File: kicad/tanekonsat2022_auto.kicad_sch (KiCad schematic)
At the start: 52 parts

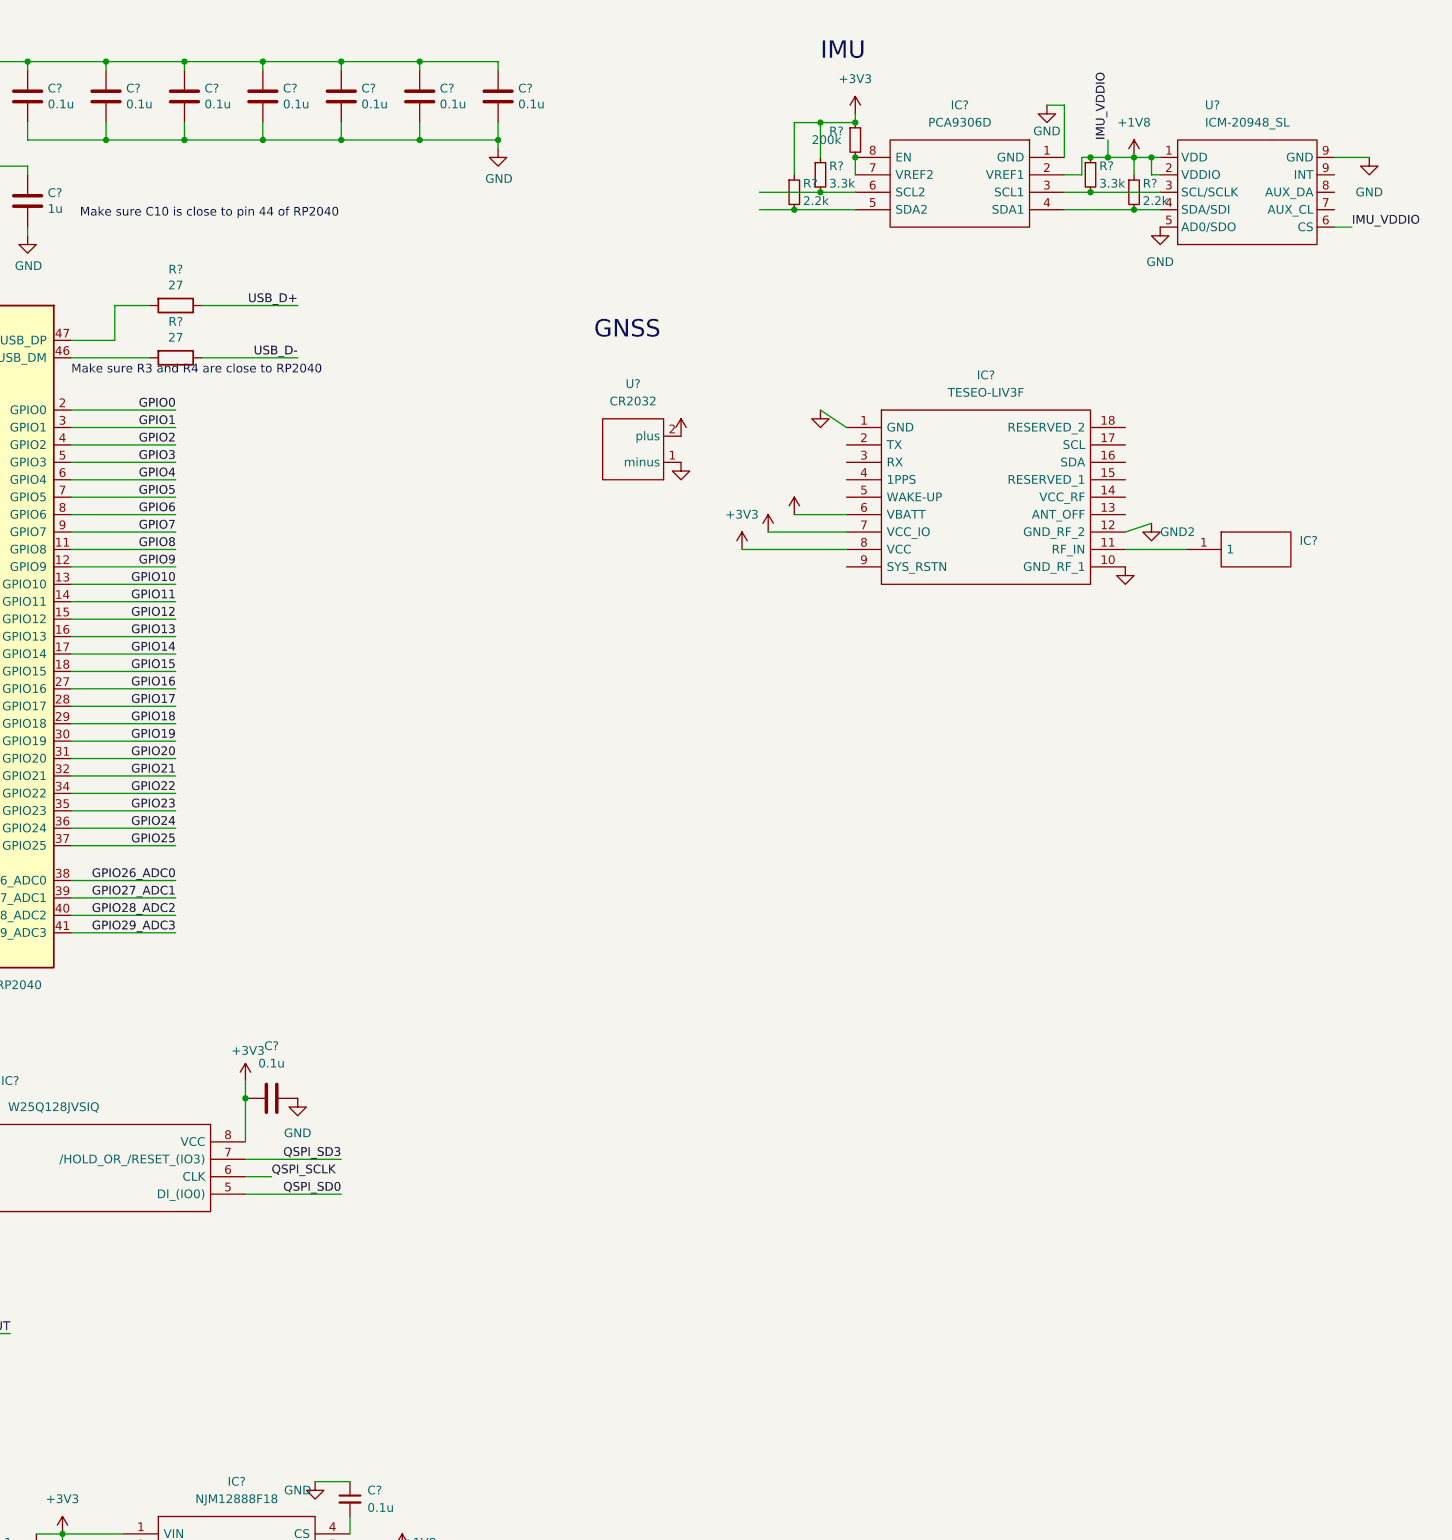
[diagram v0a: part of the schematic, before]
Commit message: update schematic
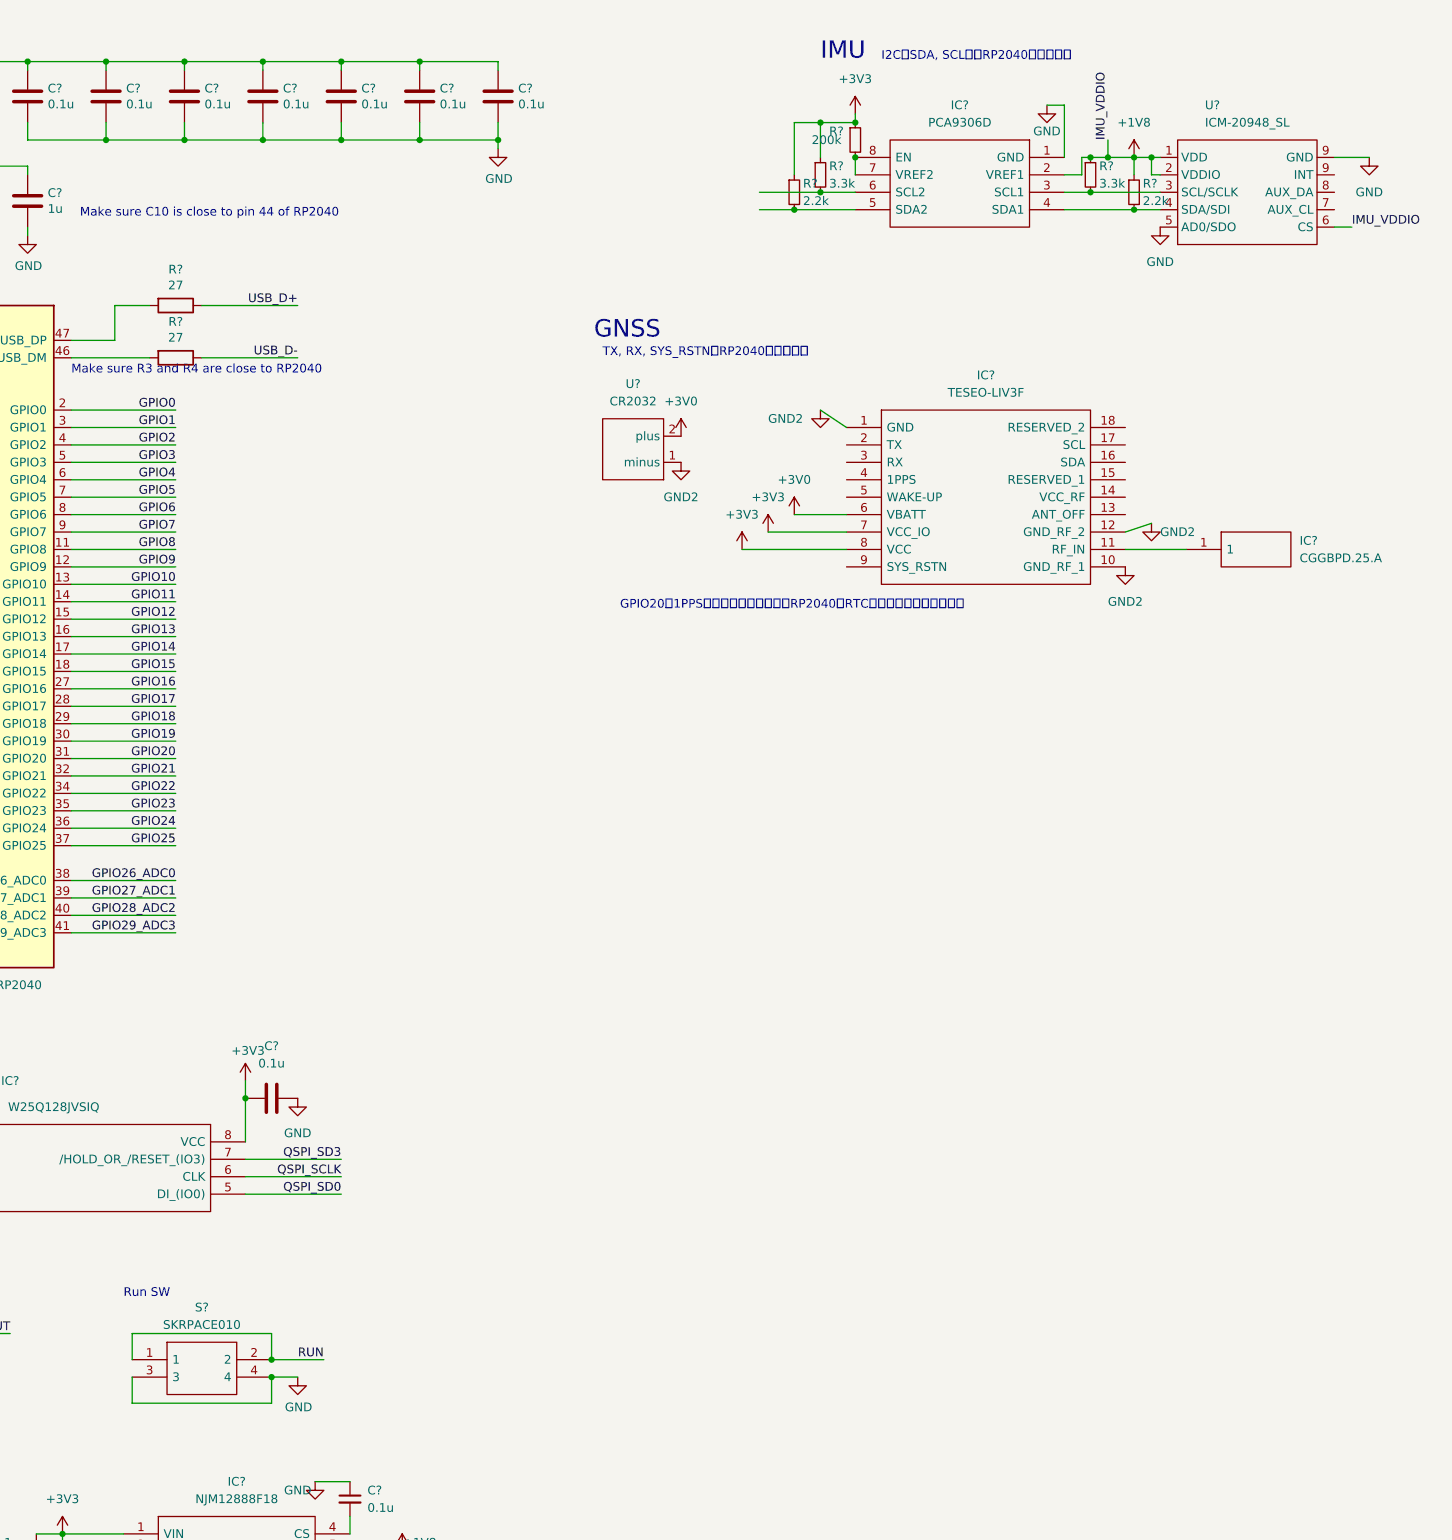
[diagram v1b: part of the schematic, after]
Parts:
- added S?: SKRPACE010, SamacSys_Parts:SMT_4.2X3.2_, symbol SamacSys_Parts:SKRPACE010
- IC?: value (none) -> CGGBPD.25.A; footprint (none) -> CGGBPD25A
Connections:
- net GND: now also S?.3, S?.4
- net RUN: now also S?.1, S?.2
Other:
- note added: "GPIO20に1PPSの信号を突っ込めば，RP2040のRTCがより高精度になるぽい"
- note added: "I2C（SDA, SCL）をRP2040と接続する"
- note added: "Run SW"
- note added: "TX, RX, SYS_RSTNをRP2040と接続する"
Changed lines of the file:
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@@
   (junction (at 252.73 38.1) (diameter 0) (color 0 0 0 0)
   )
+  (junction (at 124.46 213.36) (diameter 0) (color 0 0 0 0)
+  )
   (junction (at 35.56 259.08) (diameter 0) (color 0 0 0 0)
   )
@@
   (junction (at 123.19 35.56) (diameter 0) (color 0 0 0 0)
   )
+  (junction (at 124.46 215.9) (diameter 0) (color 0 0 0 0)
+  )
   (junction (at 123.19 24.13) (diameter 0) (color 0 0 0 0)
   )
@@
     (stroke (width 0) (type default) (color 0 0 0 0))
   )
+  (wire (pts (xy 104.14 219.71) (xy 104.14 215.9))
+    (stroke (width 0) (type default) (color 0 0 0 0))
+  )
   (wire (pts (xy 95.25 118.11) (xy 110.49 118.11))
     (stroke (width 0) (type default) (color 0 0 0 0))
@@
     (stroke (width 0) (type default) (color 0 0 0 0))
   )
+  (wire (pts (xy 128.27 215.9) (xy 124.46 215.9))
+    (stroke (width 0) (type default) (color 0 0 0 0))
+  )
   (wire (pts (xy 196.85 92.71) (xy 208.28 92.71))
     (stroke (width 0) (type default) (color 0 0 0 0))
@@
     (stroke (width 0) (type default) (color 0 0 0 0))
   )
+  (wire (pts (xy 124.46 215.9) (xy 124.46 219.71))
+    (stroke (width 0) (type default) (color 0 0 0 0))
+  )
   (wire (pts (xy 46.99 276.86) (xy 46.99 278.13))
     (stroke (width 0) (type default) (color 0 0 0 0))
@@
     (stroke (width 0) (type default) (color 0 0 0 0))
   )
+  (wire (pts (xy 132.08 213.36) (xy 124.46 213.36))
+    (stroke (width 0) (type default) (color 0 0 0 0))
+  )
   (wire (pts (xy 120.65 172.72) (xy 120.65 175.26))
     (stroke (width 0) (type default) (color 0 0 0 0))
@@
     (stroke (width 0) (type default) (color 0 0 0 0))
   )
+  (wire (pts (xy 124.46 209.55) (xy 124.46 213.36))
+    (stroke (width 0) (type default) (color 0 0 0 0))
+  )
   (wire (pts (xy 77.47 265.43) (xy 77.47 266.7))
     (stroke (width 0) (type default) (color 0 0 0 0))
@@
     (stroke (width 0) (type default) (color 0 0 0 0))
   )
+  (wire (pts (xy 124.46 209.55) (xy 104.14 209.55))
+    (stroke (width 0) (type default) (color 0 0 0 0))
+  )
   (wire (pts (xy 80.01 24.13) (xy 80.01 39.37))
     (stroke (width 0) (type default) (color 0 0 0 0))
@@
     (stroke (width 0) (type default) (color 0 0 0 0))
   )
+  (wire (pts (xy 124.46 219.71) (xy 104.14 219.71))
+    (stroke (width 0) (type default) (color 0 0 0 0))
+  )
   (wire (pts (xy 95.25 123.19) (xy 110.49 123.19))
     (stroke (width 0) (type default) (color 0 0 0 0))
@@
     (stroke (width 0) (type default) (color 0 0 0 0))
   )
+  (wire (pts (xy 104.14 209.55) (xy 104.14 213.36))
+    (stroke (width 0) (type default) (color 0 0 0 0))
+  )
   (wire (pts (xy 17.78 80.01) (xy 31.75 80.01))
     (stroke (width 0) (type default) (color 0 0 0 0))
@@
     (stroke (width 0) (type default) (color 0 0 0 0))
   )
-  (wire (pts (xy 124.46 186.69) (xy 120.65 186.69))
+  (wire (pts (xy 134.62 186.69) (xy 120.65 186.69))
     (stroke (width 0) (type default) (color 0 0 0 0))
   )
@@
     (effects (font (size 1.27 1.27)) (justify left bottom))
   )
+  (text "TX, RX, SYS_RSTNをRP2040と接続する" (at 172.72 67.31 0)
+    (effects (font (size 1.27 1.27)) (justify left bottom))
+  )
+  (text "GPIO20に1PPSの信号を突っ込めば，RP2040のRTCがより高精度になるぽい" (at 175.26 104.14 0)
+    (effects (font (size 1.27 1.27)) (justify left bottom))
+  )
   (text "Flash" (at 67.31 176.53 0)
     (effects (font (size 2.54 2.54)) (justify left bottom))
@@
     (effects (font (size 1.27 1.27)) (justify left bottom))
   )
+  (text "Run SW" (at 102.87 204.47 0)
+    (effects (font (size 1.27 1.27)) (justify left bottom))
+  )
   (text "Power" (at 33.02 231.14 0)
     (effects (font (size 2.54 2.54)) (justify left bottom))
@@
     (effects (font (size 2.54 2.54)) (justify left bottom))
   )
+  (text "I2C（SDA, SCL）をRP2040と接続する" (at 213.36 24.13 0)
+    (effects (font (size 1.27 1.27)) (justify left bottom))
+  )
   (text "IMU" (at 204.47 24.13 0)
     (effects (font (size 2.54 2.54)) (justify left bottom))
@@
     (effects (font (size 1.27 1.27)) (justify right bottom))
   )
-  (label "QSPI_SCLK" (at 124.46 186.69 0)
-    (effects (font (size 1.27 1.27)) (justify left bottom))
+  (label "QSPI_SCLK" (at 134.62 186.69 180)
+    (effects (font (size 1.27 1.27)) (justify right bottom))
   )
   (label "GPIO10" (at 110.49 100.33 180)
@@
     (effects (font (size 1.27 1.27)) (justify left bottom))
   )
+  (label "RUN" (at 132.08 213.36 180)
+    (effects (font (size 1.27 1.27)) (justify right bottom))
+  )
   (label "GPIO4" (at 110.49 85.09 180)
     (effects (font (size 1.27 1.27)) (justify right bottom))
@@
       (effects (font (size 1.27 1.27)) hide)
     )
-    (property "Value" "" (id 1) (at 184.15 87.63 0))
+    (property "Value" "GND2" (id 1) (at 184.15 87.63 0))
     (property "Footprint" "" (id 2) (at 184.15 82.55 0)
       (effects (font (size 1.27 1.27)) hide)
@@
     (pin "2")
   )
+  (symbol (lib_id "SamacSys_Parts:SKRPACE010") (at 104.14 213.36 0) (unit 1)
+    (in_bom yes) (on_board yes) (fields_autoplaced)
+    (property "Reference" "S?" (id 0) (at 114.3 205.74 0))
+    (property "Value" "SKRPACE010" (id 1) (at 114.3 208.28 0))
+    (property "Footprint" "SamacSys_Parts:SMT_4.2X3.2_" (id 2) (at 120.65 210.82 0)
+      (effects (font (size 1.27 1.27)) (justify left) hide)
+    )
+    (property "Datasheet" "http://www.alps.com/prod/info/E/HTML/Tact/SurfaceMount/SKRP/SKRPACE010.html" (id 3) (at 120.65 213.36 0)
+      (effects (font (size 1.27 1.27)) (justify left) hide)
+    )
+    (property "Description" "Tactile Switches 4.2x3.2x2.5mm 260gf" (id 4) (at 120.65 215.9 0)
+      (effects (font (size 1.27 1.27)) (justify left) hide)
+    )
+    (property "Height" "" (id 5) (at 120.65 218.44 0)
+      (effects (font (size 1.27 1.27)) (justify left) hide)
+    )
+    (property "Manufacturer_Name" "ALPS Electric" (id 6) (at 120.65 220.98 0)
+      (effects (font (size 1.27 1.27)) (justify left) hide)
+    )
+    (property "Manufacturer_Part_Number" "SKRPACE010" (id 7) (at 120.65 223.52 0)
+      (effects (font (size 1.27 1.27)) (justify left) hide)
+    )
+    (property "Mouser Part Number" "688-SKRPACE010" (id 8) (at 120.65 226.06 0)
+      (effects (font (size 1.27 1.27)) (justify left) hide)
+    )
+    (property "Mouser Price/Stock" "https://www.mouser.co.uk/ProductDetail/Alps-Alpine/SKRPACE010?qs=dHDuPHwQO79W8iY66hDbLQ%3D%3D" (id 9) (at 120.65 228.6 0)
+      (effects (font (size 1.27 1.27)) (justify left) hide)
+    )
+    (property "Arrow Part Number" "SKRPACE010" (id 10) (at 120.65 231.14 0)
+      (effects (font (size 1.27 1.27)) (justify left) hide)
+    )
+    (property "Arrow Price/Stock" "https://www.arrow.com/en/products/skrpace010/alps-electric" (id 11) (at 120.65 233.68 0)
+      (effects (font (size 1.27 1.27)) (justify left) hide)
+    )
+    (pin "1")
+    (pin "2")
+    (pin "3")
+    (pin "4")
+  )
   (symbol (lib_id "power:GND") (at 128.27 175.26 0) (unit 1)
     (in_bom yes) (on_board yes) (fields_autoplaced)
@@
     (pin "1")
   )
+  (symbol (lib_id "power:GND") (at 128.27 215.9 0) (unit 1)
+    (in_bom yes) (on_board yes)
+    (property "Reference" "#PWR?" (id 0) (at 128.27 222.25 0)
+      (effects (font (size 1.27 1.27)) hide)
+    )
+    (property "Value" "GND" (id 1) (at 128.397 220.2942 0))
+    (property "Footprint" "" (id 2) (at 128.27 215.9 0)
+      (effects (font (size 1.27 1.27)) hide)
+    )
+    (property "Datasheet" "" (id 3) (at 128.27 215.9 0)
+      (effects (font (size 1.27 1.27)) hide)
+    )
+    (pin "1")
+  )
   (symbol (lib_id "Device:C") (at 146.05 29.21 0) (unit 1)
     (in_bom yes) (on_board yes)
@@
       (effects (font (size 1.27 1.27)) hide)
     )
-    (property "Value" "" (id 1) (at 248.92 102.87 0))
+    (property "Value" "GND2" (id 1) (at 248.92 102.87 0))
     (property "Footprint" "" (id 2) (at 248.92 97.79 0)
       (effects (font (size 1.27 1.27)) hide)
@@
       (effects (font (size 1.27 1.27)) (justify left))
     )
-    (property "Value" "" (id 1) (at 274.32 96.5199 0)
+    (property "Value" "CGGBPD.25.A" (id 1) (at 274.32 96.5199 0)
       (effects (font (size 1.27 1.27)) (justify left))
     )
-    (property "Footprint" "" (id 2) (at 274.32 92.71 0)
+    (property "Footprint" "CGGBPD25A" (id 2) (at 274.32 92.71 0)
       (effects (font (size 1.27 1.27)) (justify left) hide)
     )
@@
       (effects (font (size 1.27 1.27)) hide)
     )
-    (property "Value" "" (id 1) (at 184.15 73.66 0))
+    (property "Value" "+3V0" (id 1) (at 184.15 73.66 0))
     (property "Footprint" "" (id 2) (at 184.15 78.74 0)
       (effects (font (size 1.27 1.27)) hide)
@@
       (effects (font (size 1.27 1.27)) hide)
     )
-    (property "Value" "" (id 1) (at 200.66 85.09 0))
+    (property "Value" "+3V0" (id 1) (at 200.66 85.09 0))
     (property "Footprint" "" (id 2) (at 200.66 90.17 0)
       (effects (font (size 1.27 1.27)) hide)
@@
       (effects (font (size 1.27 1.27)) hide)
     )
-    (property "Value" "" (id 1) (at 196.85 87.63 0))
+    (property "Value" "+3V3" (id 1) (at 196.85 87.63 0))
     (property "Footprint" "" (id 2) (at 196.85 92.71 0)
       (effects (font (size 1.27 1.27)) hide)
@@
       (effects (font (size 1.27 1.27)) hide)
     )
-    (property "Value" "" (id 1) (at 199.39 76.2 0))
+    (property "Value" "GND2" (id 1) (at 199.39 76.2 0))
     (property "Footprint" "" (id 2) (at 204.47 74.93 0)
       (effects (font (size 1.27 1.27)) hide)
@@
       (reference "#PWR?") (unit 1) (value "GND") (footprint "")
     )
+    (path "/8c10ccac-8385-40ea-a731-4199715c15e0"
+      (reference "#PWR?") (unit 1) (value "GND") (footprint "")
+    )
     (path "/8ede69d7-07a3-46eb-b4d4-4f95369d128e"
       (reference "#PWR?") (unit 1) (value "+1V1") (footprint "")
@@
       (reference "R?") (unit 1) (value "27") (footprint "Capacitor_SMD:C_0402_1005Metric")
     )
+    (path "/6c7c257c-43ea-4df0-bd5e-2ec621e622d0"
+      (reference "S?") (unit 1) (value "SKRPACE010") (footprint "SamacSys_Parts:SMT_4.2X3.2_")
+    )
     (path "/9b56cd8a-ebf9-458b-b49c-011cd1959228"

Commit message: update IMU level shift
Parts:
- added D?: LED, symbol Device:LED
- added IC? (x2): TB67H450FNG,EL, SOIC127P600X175-9N, symbol SamacSys_Parts:TB67H450FNG,EL
- added M? (x2): Motor_DC, symbol Motor:Motor_DC
- added Q?: (no value), symbol SamacSys_Parts:BSS138
- added Q? (x3): BSS138, SOT95P240X120-3N, symbol SamacSys_Parts:BSS138
- added R? (x4): R, symbol Device:R
- added R? (x7): 10k, symbol Device:R_Small
- added R?: 660, symbol Device:R
- added R?: (no value), symbol Device:R_Small
- added R?: 10k, symbol Device:R
- added U?: ICM-20948_SL, tanekonsat:ICM-20948_SL, symbol tanekonsat:ICM-20948_SL
- added U?: VL53L5X_SL, symbol tanekonsat:VL53L5X_SL
- IC?: footprint CGGBPD25A -> SamacSys_Parts:CGGBPD25A
- U?: footprint (none) -> tanekonsat:CR2032
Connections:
- net +1V8: now also Q?.1, Q?.1, Q?.1, Q?.1, R?.1, R?.1, R?.1, R?.1, U?.1 (VDD), U?.2 (VDDIO)
- net +3V3: now also IC?.4 (VREF), IC?.4 (VREF), R?.1, R?.1, R?.1, R?.1, R?.1, U?.5 (VDD)
- net +7V4: now also IC?.5 (VM), IC?.5 (VM)
- net GND: now also D?.1 (K), U?.6 (GND), U?.9 (INT)
- net GPIO25: now also R?.1
- net QSPI_SS: now also R?.2
- new net: IC?.7 (RS), R?.2, R?.2 (x2)
- new net: D?.2 (A), R?.2
- new net: IC?.6 (OUT1), M?.2 (-) (x2)
- new net: IC?.8 (OUT2), M?.1 (+) (x2)
- new net GND3: IC?.1 (GND), IC?.1 (GND), R?.1, R?.1, R?.1, R?.1
- new net IMU_CS: Q?.2, R?.2, U?.6 (CS)
- new net IMU_SCLK: Q?.2, R?.2, U?.3 (SCL/SCLK)
- new net IMU_SDI: Q?.2, R?.2, U?.4 (SDA/SDI)
- new net IMU_SDO: Q?.2, R?.2, U?.5 (AD0/SDO)
- new net M_CS: Q?.3, R?.2
- new net M_SCLK: Q?.3, R?.2
- new net M_SDI: Q?.3, R?.2
- new net M_SDO: Q?.3, R?.2
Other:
- note added: "I2C（SDA, SCL）をRP2040と接続する I2CよりSPIの方がよいか…"
- note added: "LED"
- note added: "LPnは低電力待機時のI2C通信オン・オフ切り替え用 RSTは，0→1→0でI2Cスレーブがリセットされる"
- note added: "LV(Low Voltage)側に1V8， HV(High Voltage)側に3V3 GNDは直結でよい"
- note added: "Motor"
- note added: "NJM12888F18はVinが6V5までなので，効率悪いけど3V3から取っている．"
- note added: "Power(Battery)"
- note added: "Power(USB)"
- note added: "Run SW（出来れば載せる）"
- note added: "SDA, SCLがつながっていれば使える"
- note added: "SPIで通信なので SCLK(クロック)，SDO(IMUからのデータ出力)， SDI(IMUへのデータ入力)，CS(チップセレクト) を結線する．"
- note added: "SPIレベル変換回路"
- note added: "ToF"
- note added: "VM, RS, OUT1, OUT2は電源系につき，アートワークに要配慮． 特に，GNDはベタ． 各INピンにPWM入力．"
- note added: "テスト・デバッグ用"
- note removed: "I2C（SDA, SCL）をRP2040と接続する"
- note removed: "Power"
- note removed: "Run SW"
- moved on the sheet: C?, IC?, J?, Q?, R?, SW?, U?, Y?
